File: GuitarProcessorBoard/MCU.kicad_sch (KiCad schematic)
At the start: 57 parts, among them J301 SWD Header, J302 PWR, Q301 BC547, Q302 BC547, SW301 RST, SW302 BOOT, U301 STM32H7B0VBT6, U302 TPS63070, Y301 32MHz, Y302 32.768kHZ

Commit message: control wiring
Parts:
- removed Q301, Q302: BC547, Package_TO_SOT_THT:TO-92_Inline, symbol Transistor_BJT:BC547
- added C327, C328, C329: 10n, Capacitor_SMD:C_0805_2012Metric, symbol Device:C
- added C330, C331: 10n, symbol Device:C
- added C332: 100n, Capacitor_SMD:C_0805_2012Metric, symbol Device:C
- added Q301, Q302: BC847, Package_TO_SOT_SMD:SOT-23, symbol Transistor_BJT:BC847
- added R315, R316, R317: 22k, symbol Device:R_US
- added R318, R321: 100k, symbol Device:R_US
- added R319, R320: 47k, symbol Device:R_US
- added RV301, RV302, RV303: 100kB, symbol Device:R_Potentiometer_US
- added SW303: ENC, Rotary_Encoder:RotaryEncoder_Alps_EC11E-Switch_Vertical_H20mm_5Pin, symbol Device:RotaryEncoder_Switch
- added SW304: BACK, symbol Switch:SW_SPST
- added U303: SSD1306_OLED_128x64, Display:SSD1306_OLED_128x64, symbol Display_Graphic:SSD1306_OLED_128x64
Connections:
- net +3.3V: now also C332.2, R318.1, R319.1, R320.1, R321.1, RV301.3, RV302.3, RV303.3, U303.2 (VCC)
- net ADC_A: now also C327.1, R315.2
- net ADC_B: now also C328.1, R316.2
- net ADC_C: now also C329.1, R317.2
- net BACK_BTN: now also R321.2, SW304.2 (B)
- net DISP_SCL: now also U303.3 (SCL)
- net DISP_SDA: now also U303.4 (SDA)
- net ENC_B: now also R318.2, SW303.S2
- net ENC_L: now also C330.1, R319.2, SW303.B
- net ENC_R: now also C331.1, R320.2, SW303.A
- net GND: now also C327.2, C328.2, C329.2, C330.2, C331.2, C332.1, Q301.2 (E), Q302.2 (E), RV301.1, RV302.1, RV303.1, SW303.C, SW303.S1, SW304.1 (A), U303.1 (GND)
- net at R306.2: now also Q301.3 (C)
- net at R308.1: now also Q302.1 (B)
- net at R305.1: now also Q301.1 (B)
- net at R307.2: now also Q302.3 (C)
- new net: R317.1, RV303.2
- new net: R316.1, RV302.2
- new net: R315.1, RV301.2
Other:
- moved on the sheet: C318, D303, J301, R309, R310, SW301, SW302

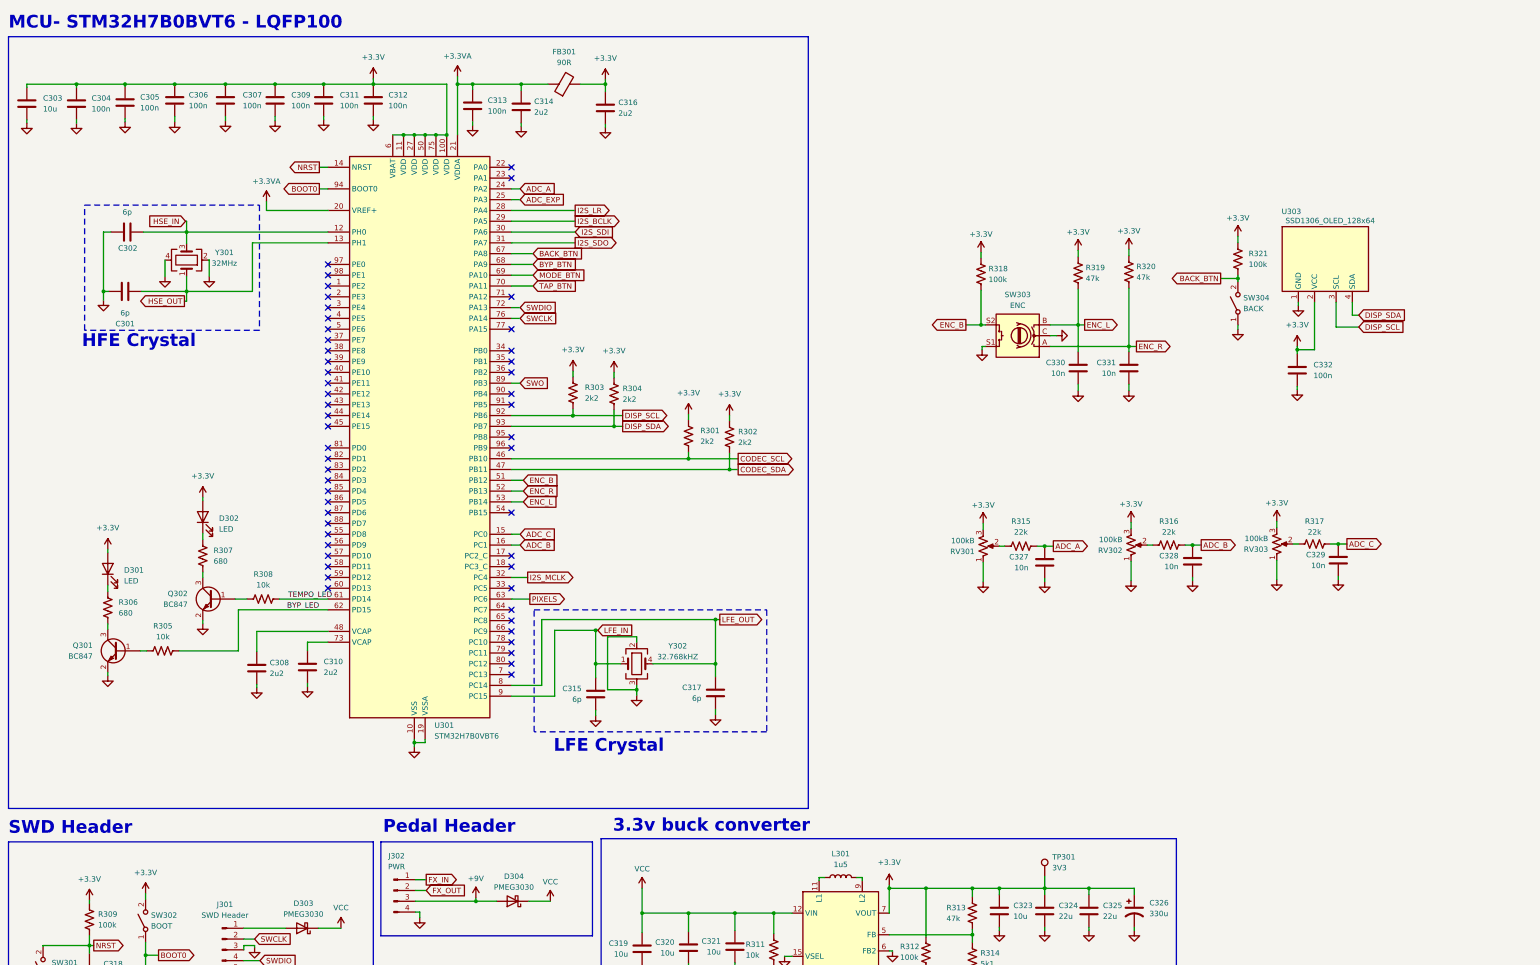
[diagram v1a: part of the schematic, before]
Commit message: switched to shift register LEDs
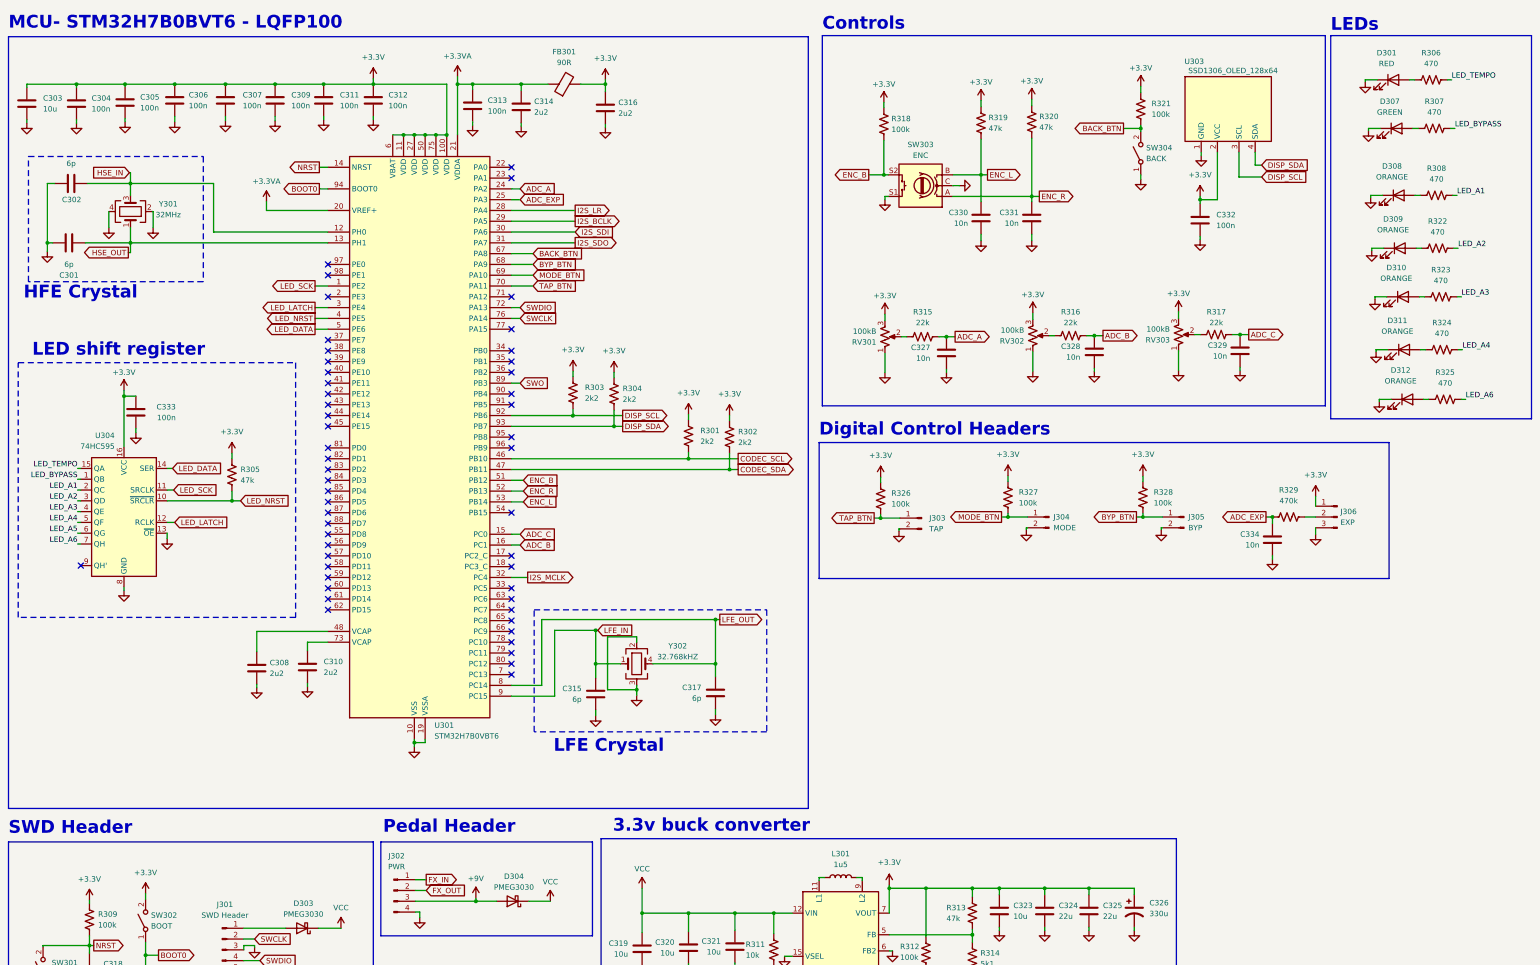
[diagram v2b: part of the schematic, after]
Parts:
- removed D302: LED, symbol Device:LED
- removed Q301, Q302: BC847, Package_TO_SOT_SMD:SOT-23, symbol Transistor_BJT:BC847
- removed TP301: 3V3, TestPoint:TestPoint_THTPad_D1.0mm_Drill0.5mm_VAL, symbol Connector:TestPoint
- added C333: 100n, Capacitor_SMD:C_0805_2012Metric, symbol Device:C
- added C334: 10n, Capacitor_SMD:C_0805_2012Metric, symbol Device:C
- added D307: GREEN, LED_THT:LED_D3.0mm, symbol Device:LED
- added D308, D309, D310, D311, D312: ORANGE, LED_THT:LED_D3.0mm, symbol Device:LED
- added J303: TAP, Connector_PinHeader_2.54mm:PinHeader_1x02_P2.54mm_Vertical, symbol Connector:Conn_01x02_Pin
- added J304: MODE, Connector_PinHeader_2.54mm:PinHeader_1x02_P2.54mm_Vertical, symbol Connector:Conn_01x02_Pin
- added J305: BYP, Connector_PinHeader_2.54mm:PinHeader_1x02_P2.54mm_Vertical, symbol Connector:Conn_01x02_Pin
- added J306: EXP, Connector_PinHeader_2.54mm:PinHeader_1x03_P2.54mm_Vertical, symbol Connector:Conn_01x03_Pin
- added R322, R323, R324, R325: 470, symbol Device:R_US
- added R326, R327, R328: 100k, symbol Device:R_US
- added R329: 470k, symbol Device:R_US
- added U304: 74HC595, Package_SO:SOIC-16_3.9x9.9mm_P1.27mm, symbol 74xx:74HC595
- D301: value LED -> RED; footprint (none) -> LED_THT:LED_D3.0mm
- R305: value 10k -> 47k
- R306, R307: value 680 -> 470
- R308: value 10k -> 470
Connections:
- net +3.3V: now also R305.1, C333.1, J306.1 (Pin_1), R326.1, R327.1, R328.1, U304.16 (VCC); no longer D301.2 (A)
- net ADC_EXP: now also C334.1, R329.1
- net BYP_BTN: now also J305.1 (Pin_1), R328.2
- net GND: now also D301.1 (K), C333.2, C334.2, D307.1 (K), D308.1 (K), D309.1 (K), D310.1 (K), D311.1 (K), D312.1 (K), J303.2 (Pin_2), J304.2 (Pin_2), J305.2 (Pin_2), J306.3 (Pin_3), U304.13 (~{OE}), U304.8 (GND)
- net MODE_BTN: now also J304.1 (Pin_1), R327.2
- net TAP_BTN: now also J303.1 (Pin_1), R326.2
- net at R306.1: now also D301.2 (A); no longer D301.1 (K)
- net LED_TEMPO: now reaches R306.2
- net LED_TEMPO: now also U304.15 (QA)
- net at R308.1: now also D308.2 (A)
- net LED_SCK: now reaches U301.1 (PE2)
- net LED_SCK: now also U304.11 (SRCLK)
- net LED_LATCH: now reaches U301.3 (PE4)
- net LED_LATCH: now also U304.12 (RCLK)
- net LED_NRST: now reaches U301.4 (PE5)
- net LED_NRST: now also R305.2, U304.10 (~{SRCLR})
- net LED_DATA: now reaches U301.5 (PE6)
- net LED_DATA: now also U304.14 (SER)
- net LED_BYPASS: now reaches R307.2
- net LED_BYPASS: now also U304.1 (QB)
- net at R307.1: now also D307.2 (A)
- net BYP_LED: no longer names the net of U301.62 (PD15)
- net BYP_LED: no longer R305.2
- net PIXELS: no longer names the net of U301.63 (PC6)
- net TEMPO_LED: no longer names the net of U301.61 (PD14)
- net TEMPO_LED: no longer R308.2
- new net: J306.2 (Pin_2), R329.2
- new net: D311.2 (A), R324.1
- new net: D310.2 (A), R323.1
- new net: D309.2 (A), R322.1
- new net: D312.2 (A), R325.1
- new net LED_A1: R308.2, U304.2 (QC)
- new net LED_A2: R322.2, U304.3 (QD)
- new net LED_A3: R323.2, U304.4 (QE)
- new net LED_A4: R324.2, U304.5 (QF)
- new net LED_A5: U304.6 (QG)
- new net LED_A6: R325.2, U304.7 (QH)
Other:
- note added: "Controls"
- note added: "Digital Control Headers"
- note added: "LED shift register"
- note added: "LEDs"
- moved on the sheet: C301, C302, C327, C328, C329, C330, C331, C332, R315, R316, R317, R318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

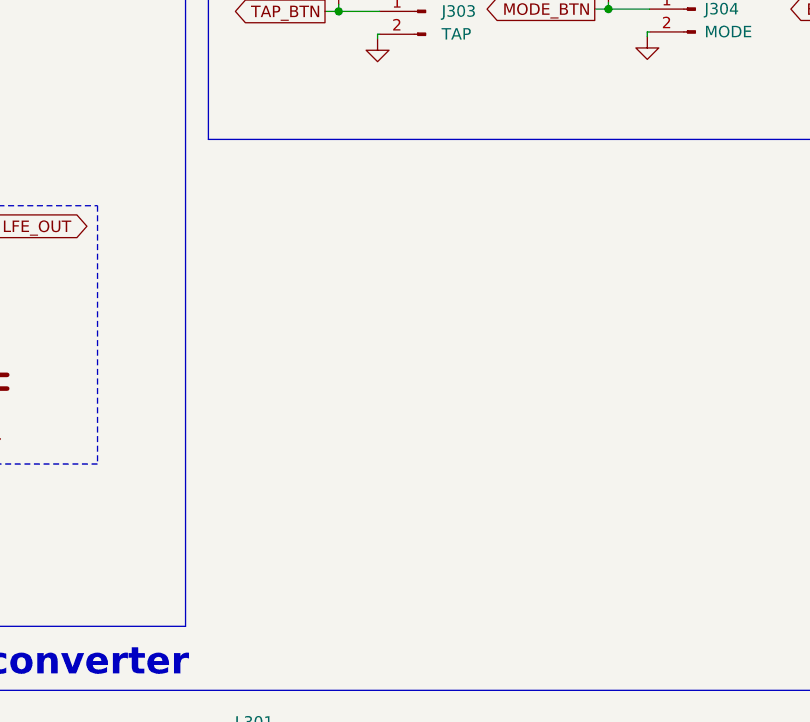
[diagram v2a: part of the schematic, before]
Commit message: added analog wet/dry control
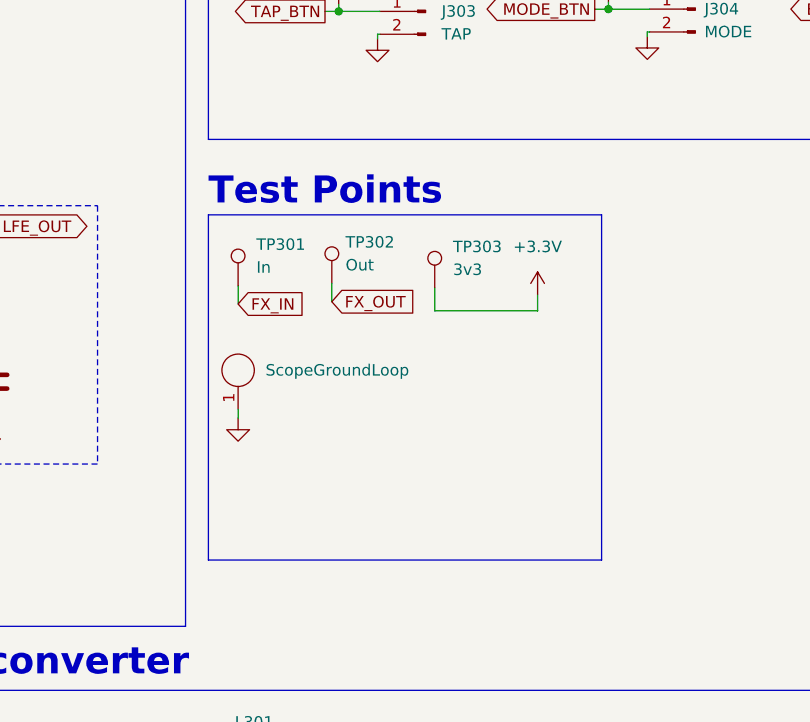
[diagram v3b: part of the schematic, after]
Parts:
- added J307: ScopeGroundLoop, Connector:THT_GND_WIRE, symbol Connector:ScopeGroundLoop
- added TP301: In, TestPoint:TestPoint_THTPad_D2.0mm_Drill1.0mm_VAL, symbol Connector:TestPoint
- added TP302: Out, TestPoint:TestPoint_THTPad_D2.0mm_Drill1.0mm_VAL, symbol Connector:TestPoint
- added TP303: 3v3, TestPoint:TestPoint_THTPad_D2.0mm_Drill1.0mm_VAL, symbol Connector:TestPoint
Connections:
- net +3.3V: now also TP303.1
- net FX_IN: now also TP301.1
- net FX_OUT: now also TP302.1
- net GND: now also J307.1
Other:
- note added: "Test Points"

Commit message: control/ enclosure layout
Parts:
- C330, C331: footprint (none) -> Capacitor_SMD:C_0805_2012Metric
- R301, R302, R303, R304, R305, R306, R307, R308, R315, R316, R317, R318, R319, R320, R321, R322, R323, R324, R325, R326, R327, R328, R329: footprint (none) -> Resistor_SMD:R_0805_2012Metric
- RV301, RV302, RV303: footprint (none) -> Potentiometer_THT:Potentiometer_Alpha_RV16AF_42_Single_Long
- SW304: footprint (none) -> Button_Switch_THT:SW_PUSH_6mm
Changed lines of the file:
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@@
 			)
 		)
-		(property "Footprint" ""
+		(property "Footprint" "Resistor_SMD:R_0805_2012Metric"
 			(at 157.226 106.426 90)
 			(effects
@@
 			)
 		)
-		(property "Footprint" ""
+		(property "Footprint" "Resistor_SMD:R_0805_2012Metric"
 			(at 259.588 131.064 90)
 			(effects
@@
 			)
 		)
-		(property "Footprint" ""
+		(property "Footprint" "Resistor_SMD:R_0805_2012Metric"
 			(at 194.056 116.84 90)
 			(effects
@@
 			)
 		)
-		(property "Footprint" ""
+		(property "Footprint" "Resistor_SMD:R_0805_2012Metric"
 			(at 290.83 39.624 90)
 			(effects
@@
 			)
 		)
-		(property "Footprint" ""
+		(property "Footprint" "Capacitor_SMD:C_0805_2012Metric"
 			(at 251.2568 68.834 0)
 			(effects
@@
 			)
 		)
-		(property "Footprint" ""
+		(property "Footprint" "Resistor_SMD:R_0805_2012Metric"
 			(at 76.962 125.73 90)
 			(effects
@@
 			)
 		)
-		(property "Footprint" ""
+		(property "Footprint" "Resistor_SMD:R_0805_2012Metric"
 			(at 184.404 116.586 90)
 			(effects
@@
 			)
 		)
-		(property "Footprint" ""
+		(property "Footprint" "Resistor_SMD:R_0805_2012Metric"
 			(at 265.176 42.672 90)
 			(effects
@@
 			)
 		)
-		(property "Footprint" ""
+		(property "Footprint" "Capacitor_SMD:C_0805_2012Metric"
 			(at 263.1948 68.834 0)
 			(effects
@@
 			)
 		)
-		(property "Footprint" ""
+		(property "Footprint" "Resistor_SMD:R_0805_2012Metric"
 			(at 324.866 134.366 90)
 			(effects
@@
 			)
 		)
-		(property "Footprint" ""
+		(property "Footprint" "Resistor_SMD:R_0805_2012Metric"
 			(at 291.338 131.064 90)
 			(effects
@@
 			)
 		)
-		(property "Footprint" ""
+		(property "Footprint" "Button_Switch_THT:SW_PUSH_6mm"
 			(at 289.814 49.784 0)
 			(effects
@@
 			)
 		)
-		(property "Footprint" ""
+		(property "Footprint" "Resistor_SMD:R_0805_2012Metric"
 			(at 358.394 31.496 90)
 			(effects
@@
 			)
 		)
-		(property "Footprint" ""
+		(property "Footprint" "Resistor_SMD:R_0805_2012Metric"
 			(at 359.664 58.674 90)
 			(effects
@@
 			)
 		)
-		(property "Footprint" ""
+		(property "Footprint" "Potentiometer_THT:Potentiometer_Alpha_RV16AF_42_Single_Long"
 			(at 298.704 92.456 0)
 			(effects
@@
 			)
 		)
-		(property "Footprint" ""
+		(property "Footprint" "Resistor_SMD:R_0805_2012Metric"
 			(at 359.918 71.12 90)
 			(effects
@@
 			)
 		)
-		(property "Footprint" ""
+		(property "Footprint" "Resistor_SMD:R_0805_2012Metric"
 			(at 307.848 91.44 90)
 			(effects
@@
 			)
 		)
-		(property "Footprint" ""
+		(property "Footprint" "Resistor_SMD:R_0805_2012Metric"
 			(at 229.616 131.318 90)
 			(effects
@@
 			)
 		)
-		(property "Footprint" ""
+		(property "Footprint" "Resistor_SMD:R_0805_2012Metric"
 			(at 360.934 94.996 90)
 			(effects
@@
 			)
 		)
-		(property "Footprint" ""
+		(property "Footprint" "Resistor_SMD:R_0805_2012Metric"
 			(at 359.156 42.926 90)
 			(effects
@@
 			)
 		)
-		(property "Footprint" ""
+		(property "Footprint" "Resistor_SMD:R_0805_2012Metric"
 			(at 166.878 106.68 90)
 			(effects
@@
 			)
 		)
-		(property "Footprint" ""
+		(property "Footprint" "Potentiometer_THT:Potentiometer_Alpha_RV16AF_42_Single_Long"
 			(at 264.414 92.71 0)
 			(effects
@@
 			)
 		)
-		(property "Footprint" ""
+		(property "Footprint" "Resistor_SMD:R_0805_2012Metric"
 			(at 230.378 43.18 90)
 			(effects
@@
 			)
 		)
-		(property "Footprint" ""
+		(property "Footprint" "Resistor_SMD:R_0805_2012Metric"
 			(at 253.238 42.926 90)
 			(effects
@@
 			)
 		)
-		(property "Footprint" ""
+		(property "Footprint" "Potentiometer_THT:Potentiometer_Alpha_RV16AF_42_Single_Long"
 			(at 229.616 92.964 0)
 			(effects
@@
 			)
 		)
-		(property "Footprint" ""
+		(property "Footprint" "Resistor_SMD:R_0805_2012Metric"
 			(at 360.68 82.55 90)
 			(effects
@@
 			)
 		)
-		(property "Footprint" ""
+		(property "Footprint" "Resistor_SMD:R_0805_2012Metric"
 			(at 361.696 106.68 90)
 			(effects
@@
 			)
 		)
-		(property "Footprint" ""
+		(property "Footprint" "Resistor_SMD:R_0805_2012Metric"
 			(at 273.558 91.694 90)
 			(effects
@@
 			)
 		)
-		(property "Footprint" ""
+		(property "Footprint" "Resistor_SMD:R_0805_2012Metric"
 			(at 238.76 91.948 90)
 			(effects

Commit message: starting layout
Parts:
- added R330, R331, R332, R333: 22, Resistor_SMD:R_0805_2012Metric, symbol Device:R_US
- C301, C302: value 6p -> 10p
- RV301, RV302, RV303: footprint Potentiometer_THT:Potentiometer_Alpha_RV16AF_42_Single_Long -> Potentiometer_THT:Potentiometer_Alpha_RD901F-40-00D_Single_Vertical_CircularHoles
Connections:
- net I2S_BCLK: now also R332.2; no longer U301.29 (PA5)
- net I2S_LR: now also R333.2; no longer U301.28 (PA4)
- net I2S_MCLK: now also R331.2; no longer U301.32 (PC4)
- net I2S_SDO: now also R330.2; no longer U301.31 (PA7)
- net LED_A5: now also R325.2
- net CODEC_NRST: now reaches U301.45 (PE15)
- net LED_A6: no longer names the net of U304.7 (QH)
- net LED_A6: no longer R325.2
- new net: R333.1, U301.28 (PA4)
- new net: R332.1, U301.29 (PA5)
- new net: R330.1, U301.31 (PA7)
- new net: R331.1, U301.32 (PC4)
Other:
- moved on the sheet: C301, C302, C303, C304, C305, C306, C307, C308, C309, C310, C311, C312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
